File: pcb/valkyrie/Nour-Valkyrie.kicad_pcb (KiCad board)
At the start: 4 copper layers, 145.4 x 226.5 mm, 201 parts, among them IC1 IS31FL3733B-QFLS4-TR, J1 SJ-435107RS, J2 Conn_ARM_JTAG_SWD_10, J3 USB_C_Receptacle_USB2.0, J4 USB_C_Receptacle_USB2.0, J5 SJ-435107RS, SW1 SW_SPDT, SW10 LAYER, SW11 I, SW12 K, SW13 ,, SW14 LAYER, SW15 O, SW16 L, SW17 ., SW18 LAYER, SW19 P, SW2 SW_SPST_G, SW20 ;, SW21 /, SW22 RCTRL, SW23 [, SW24 ', SW25 RSHIFT, SW26 ], SW27 ENTER, SW3 Y, SW30 ESCAPE, SW31 OSKEY, SW32 TAB, SW33 GRAVE, SW34 LEFT_SHIFT, SW35 Q, SW36 A, SW37 Z, SW38 LEFT_CTRL, SW39 W, SW4 H, SW40 S, SW41 X, SW42 LAYER1, SW43 E, SW44 D, SW45 C, SW46 LAYER2, SW47 R, SW48 F, SW49 V, SW5 N, SW50 LEFT_ALT, SW51 T, SW52 G, SW53 B, SW54 SPACE, SW6 SPACE, SW7 U, SW8 J, SW9 M, U1 STM32L082CZYx, U2 AP2112K-3.3, U3 NourK_Core, U4 NourK_Core, U5 NourK_Core, Y1 32.768KHz, Y2 8MHz

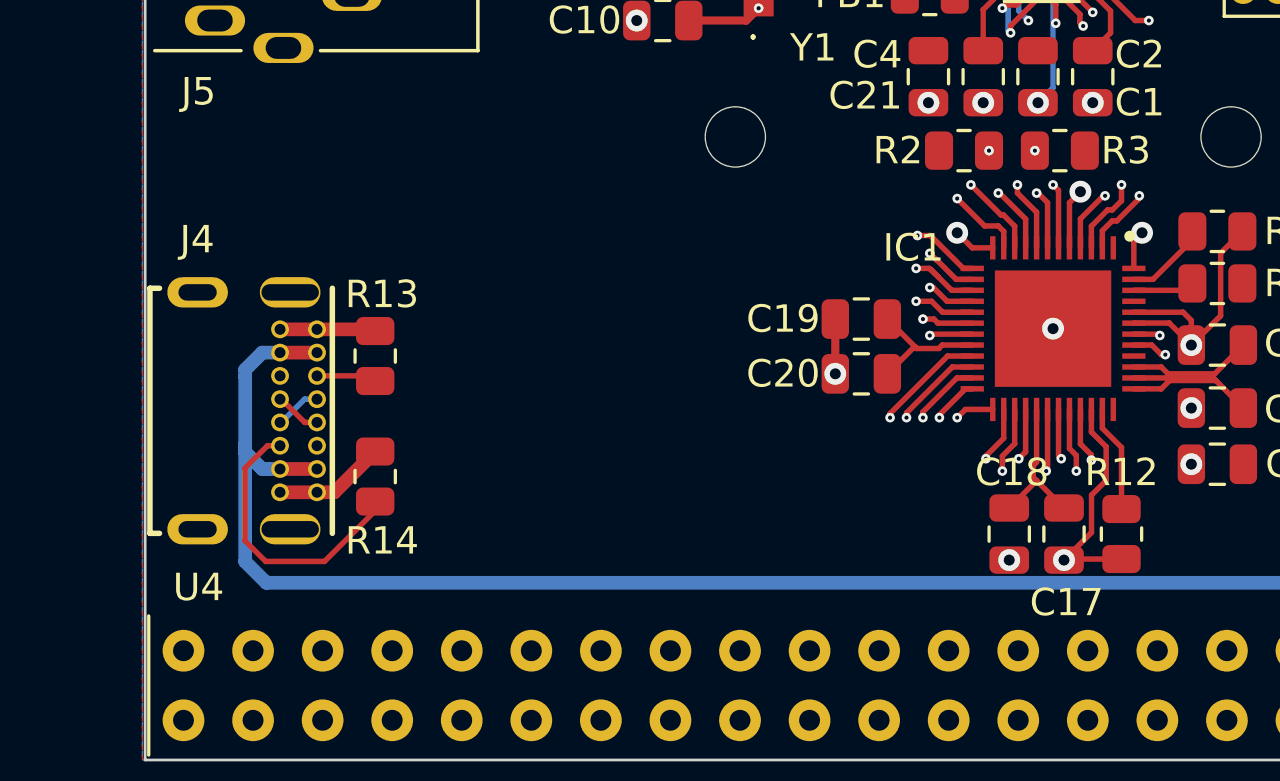
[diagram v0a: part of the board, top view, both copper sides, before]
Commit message: Rename project
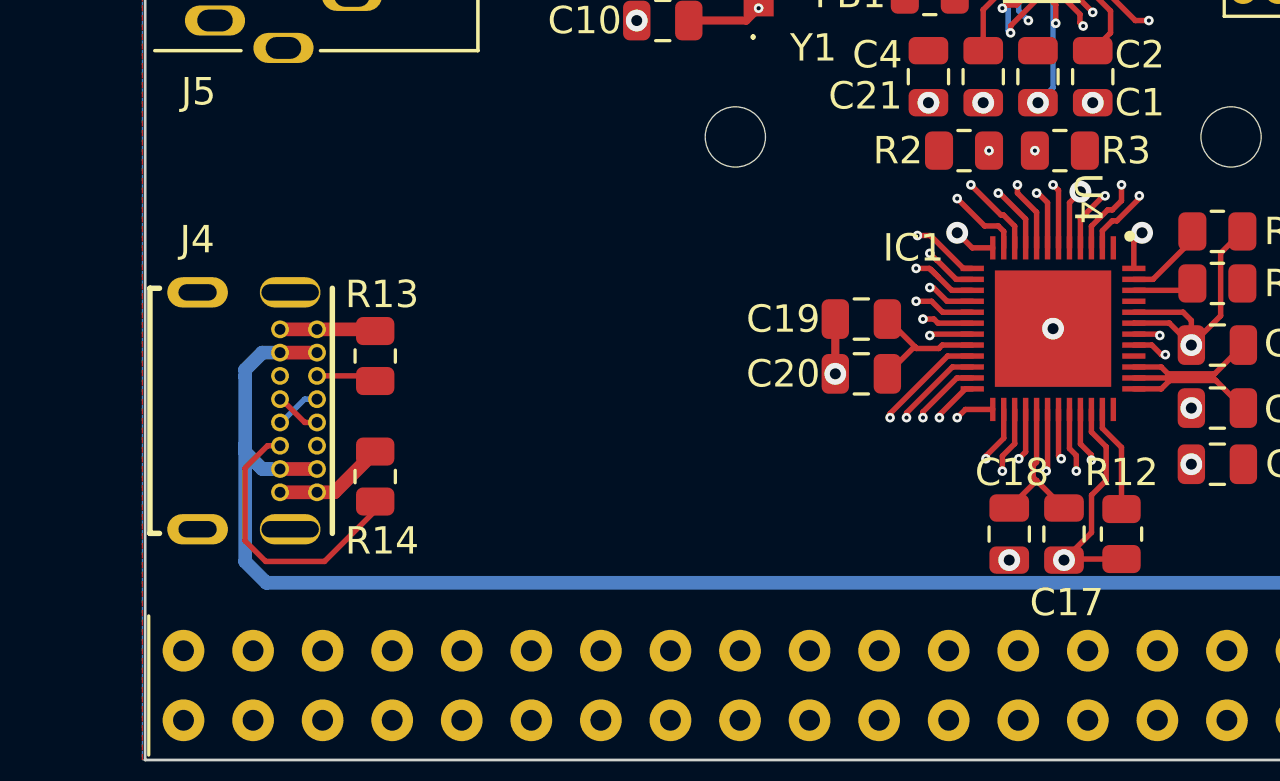
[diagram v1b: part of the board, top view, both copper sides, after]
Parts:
- U3, U4, U5: footprint Nour_KB:NourKB_Core_2 -> Nour_KB:Nour_Core

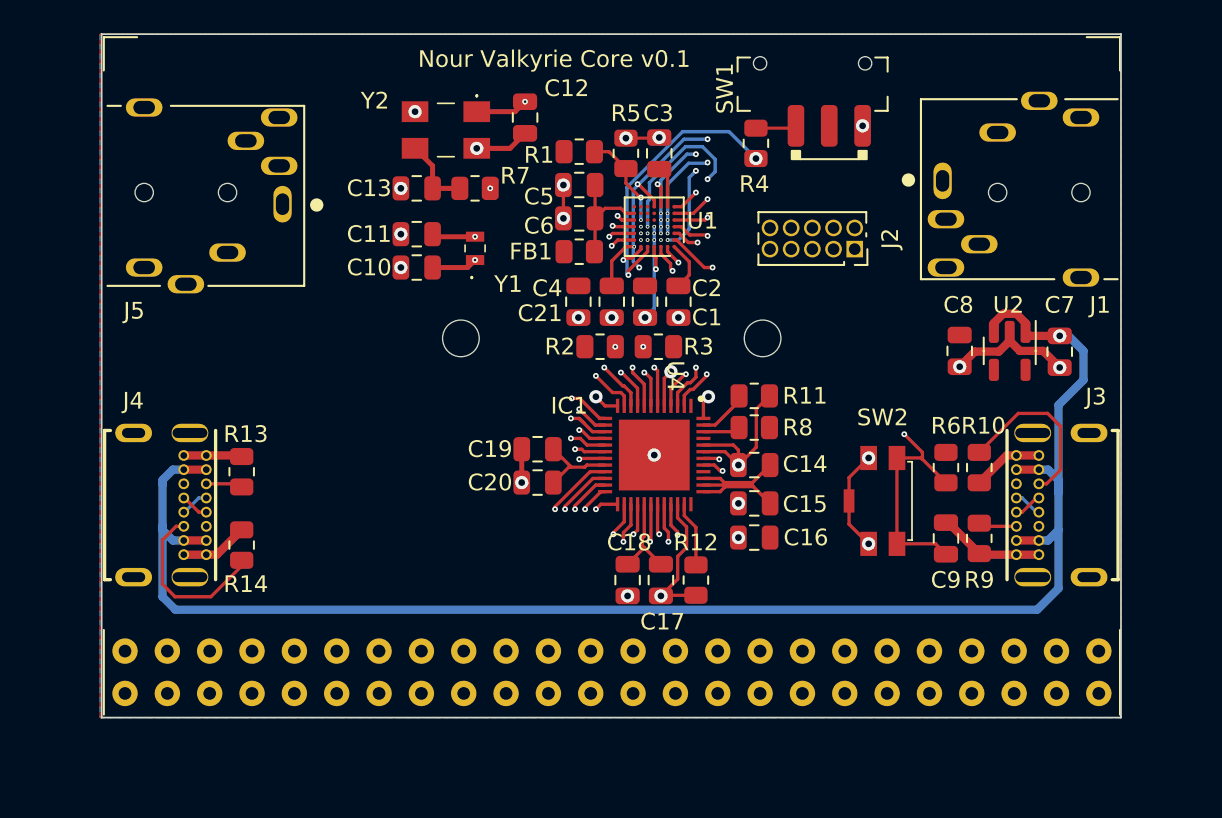
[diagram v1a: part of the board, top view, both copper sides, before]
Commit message: Split the Core into a separate project
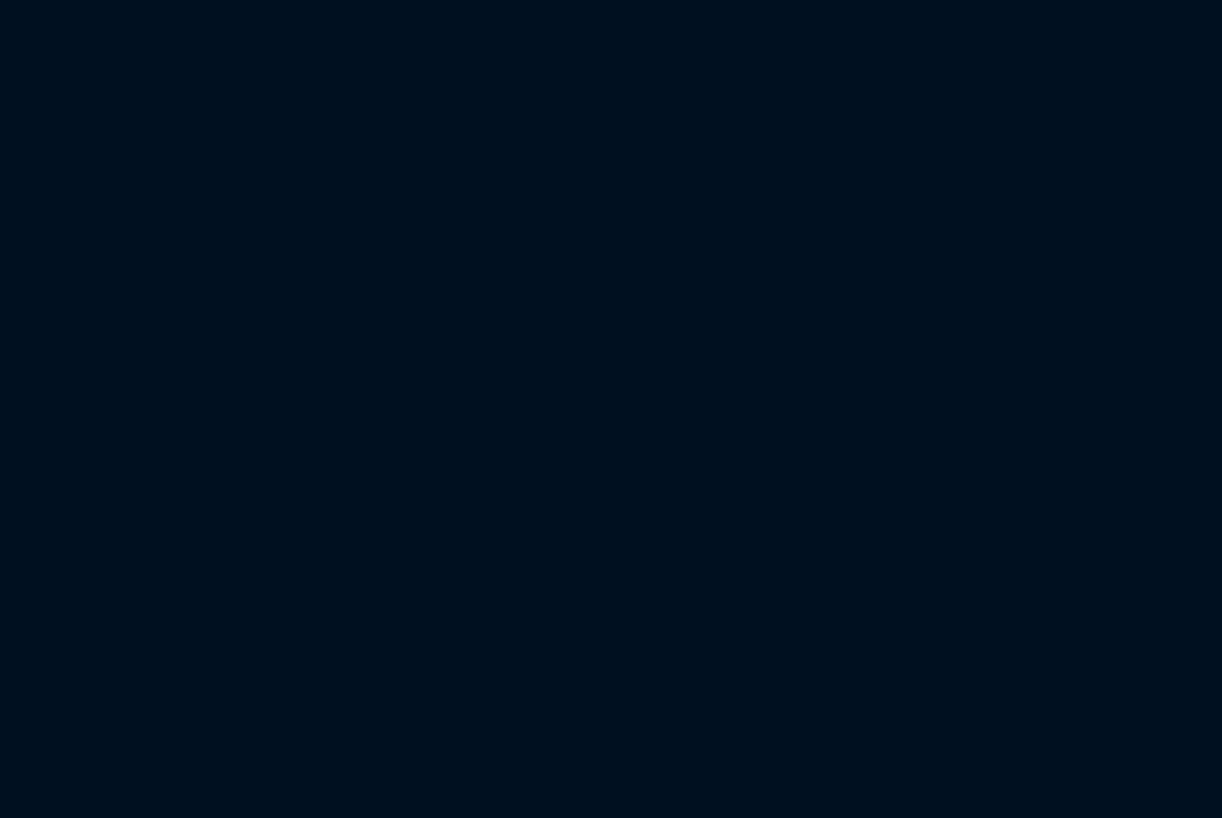
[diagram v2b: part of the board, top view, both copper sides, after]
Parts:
- removed C1, C2, C21, C3, C6: 100nF, Capacitor_SMD:C_0805_2012Metric
- removed C10, C11: 7pF, Capacitor_SMD:C_0805_2012Metric
- removed C12, C13: 10pF, Capacitor_SMD:C_0805_2012Metric
- removed C14, C15, C17, C19: 0.47uF, Capacitor_SMD:C_0805_2012Metric
- removed C16, C18, C20: 0.1uF, Capacitor_SMD:C_0805_2012Metric
- removed C4: 10uF, Capacitor_SMD:C_0805_2012Metric
- removed C5, C7, C8: 1uF, Capacitor_SMD:C_0805_2012Metric
- removed C9: 10nF, Capacitor_SMD:C_0805_2012Metric
- removed FB1: FerriteBead, Resistor_SMD:R_0805_2012Metric
- removed IC1: IS31FL3733B-QFLS4-TR, Nour_KB:QFN40P600X600X80-49N-D
- removed J1, J5: SJ-435107RS, Nour_KB:CUI_SJ-435107RS
- removed J2: Conn_ARM_JTAG_SWD_10, Connector_PinSocket_1.27mm:PinSocket_2x05_P1.27mm_Vertical
- removed J3, J4: USB_C_Receptacle_USB2.0, Nour_KB:GCT_USB4085-GF-A_REVA4
- removed R1, R4, R5: 10K, Resistor_SMD:R_0805_2012Metric
- removed R10, R13, R14, R9: 5K1, Resistor_SMD:R_0805_2012Metric
- removed R11, R6, R8: 100K, Resistor_SMD:R_0805_2012Metric
- removed R12: R, Resistor_SMD:R_0805_2012Metric
- removed R2, R3: 4k7, Resistor_SMD:R_0805_2012Metric
- removed R7: 1990, Resistor_SMD:R_0805_2012Metric
- removed the REF** at (70.4, 42.2)
- removed the REF** at (88.5, 42.2)
- removed SW1: SW_SPDT, Nour_KB:CSS-1211TB
- removed SW2: SW_SPST_G, Nour_KB:EVQP9102W
- removed U1: STM32L082CZYx, Nour_KB:ST_WLCSP-49_Die447
- removed U2: AP2112K-3.3, Package_TO_SOT_SMD:SOT-23-5
- removed U4: NourK_Core, Nour_KB:Nour_Core
- removed Y1: 32.768KHz, Nour_KB:ECS327712TR
- removed Y2: 8MHz, Nour_KB:ECS801830BAGNTR
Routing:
- net /core/D+: track 101.3 -> 0.00 mm, vias 2 -> 0
- net /core/D-: track 99.6 -> 0.00 mm, vias 1 -> 0
- net VBUS: track 96.2 -> 0.00 mm, vias 1 -> 0
- net GND: track 71.3 -> 0.00 mm, vias 29 -> 0
- net /core/USART.TX: track 67.3 -> 0.00 mm, vias 3 -> 0
- net /core/USART.RX: track 63.6 -> 0.00 mm, vias 2 -> 0
- net /core/KEY.COL2: track 52.2 -> 0.00 mm, vias 2 -> 0
- net /core/KEY.COL1: track 52.0 -> 0.00 mm, vias 1 -> 0
- net /core/KEY.COL10: track 51.7 -> 0.00 mm, vias 1 -> 0
- net /core/KEY.COL9: track 49.7 -> 0.00 mm, vias 1 -> 0
- net /core/KEY.COL8: track 48.6 -> 0.00 mm, vias 1 -> 0
- net /core/KEY.COL3: track 47.9 -> 0.00 mm, vias 1 -> 0
- net /core/KEY.COL7: track 47.7 -> 0.00 mm, vias 1 -> 0
- net /core/KEY.COL4: track 47.2 -> 0.00 mm, vias 2 -> 0
- net /core/KEY.COL6: track 46.2 -> 0.00 mm, vias 1 -> 0
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- removed copper zone on B.Cu, net GND
- removed copper zone on F.Cu, net VCC
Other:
- board size 145.4 x 226.5 mm -> 145.4 x 176.3 mm
- copper layers 4 -> 2
- board text removed: "(A) 61x41mm 4 layer PCB, 2x"
- board text removed: "Nour Valkyrie Core v0.1"
